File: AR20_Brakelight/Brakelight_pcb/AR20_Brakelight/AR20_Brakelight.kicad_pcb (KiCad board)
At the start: 2 copper layers, 58 parts, among them IC1 PAM2863ECR

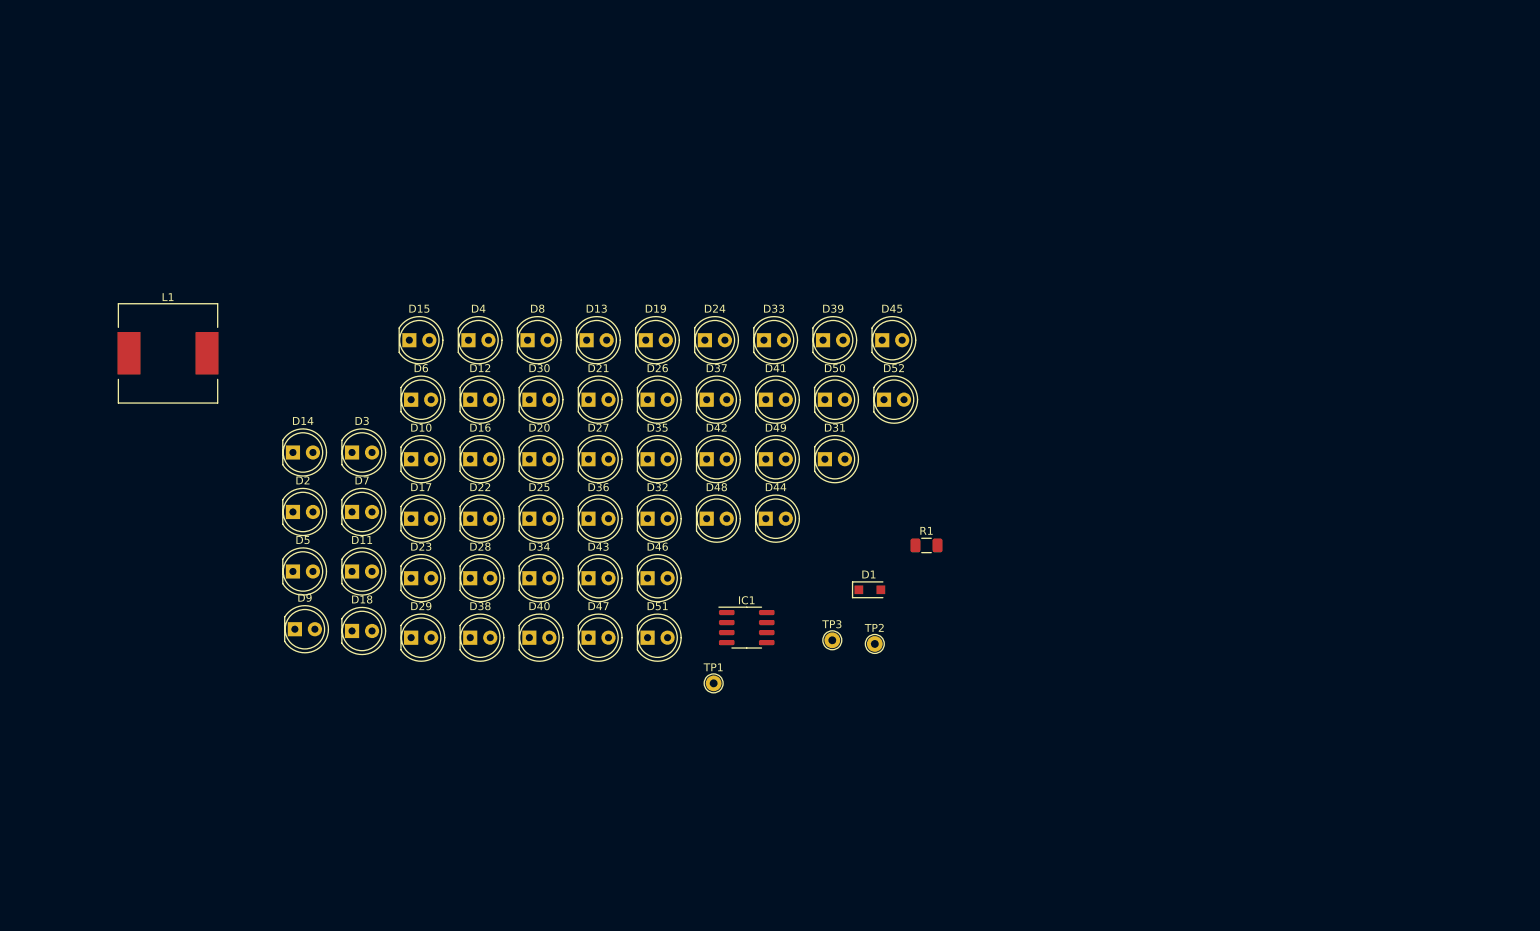
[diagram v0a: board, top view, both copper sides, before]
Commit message: Brakelight PCB 50% ready
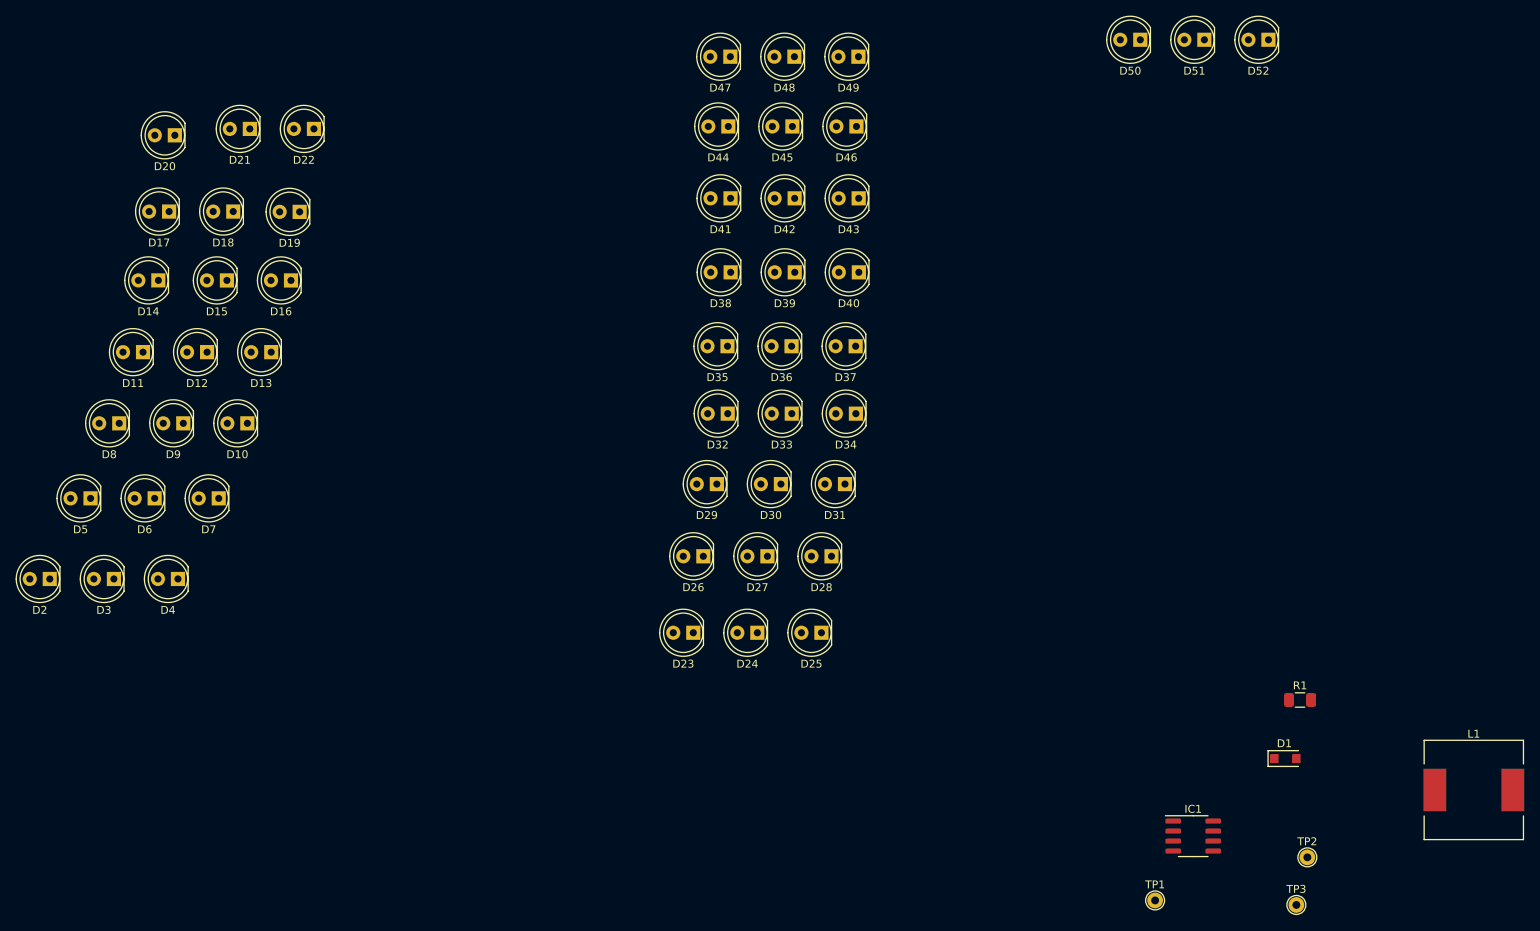
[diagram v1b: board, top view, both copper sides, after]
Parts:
- moved L1 174.7 mm to (257.2, 148.1)
- moved D51 103.7 mm to (223.0, 52.9), turned to 180 degrees
- moved D47 75.9 mm to (162.9, 55.0), turned to 180 degrees
- moved TP3 67.8 mm to (234.7, 162.7)
- moved D52 66.8 mm to (231.2, 52.9), turned to 180 degrees
- moved D46 63.2 mm to (178.9, 63.9), turned to 180 degrees
- moved IC1 62.5 mm to (221.6, 154.0)
- moved D40 62.4 mm to (179.2, 82.4), turned to 180 degrees
- moved TP1 62.4 mm to (216.8, 162.1)
- moved TP2 61.2 mm to (236.1, 156.6)
- moved D20 60.9 mm to (92.4, 65.0), turned to 180 degrees
- moved D50 60.7 mm to (214.9, 52.9), turned to 180 degrees
- moved D48 59.7 mm to (171.0, 55.0), turned to 180 degrees
- moved D43 59.2 mm to (179.2, 73.0), turned to 180 degrees
- moved D38 56.9 mm to (162.9, 82.4), turned to 180 degrees
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
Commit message: Brakelight 80% Ready
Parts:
- moved D49 95.9 mm to (124.0, 133.5), turned to 0 degrees
- moved D52 92.1 mm to (147.3, 91.1), turned to 0 degrees
- moved D48 88.1 mm to (130.7, 133.5), turned to 0 degrees
- moved D46 85.2 mm to (122.3, 127.6), turned to 0 degrees
- moved D47 82.4 mm to (137.5, 133.5), turned to 0 degrees
- moved D25 76.3 mm to (110.2, 86.9), turned to 0 degrees
- moved D43 76.3 mm to (120.6, 121.8), turned to 0 degrees
- moved D51 76.3 mm to (153.2, 83.7)
- moved D45 76.2 mm to (129.0, 127.6), turned to 0 degrees
- moved D50 75.1 mm to (146.3, 83.7)
- moved D44 69.2 mm to (135.8, 127.6), turned to 0 degrees
- moved D40 69.1 mm to (118.8, 116.0), turned to 0 degrees
- moved D28 68.8 mm to (111.9, 92.7), turned to 0 degrees
- moved D42 65.5 mm to (127.3, 121.8), turned to 0 degrees
- moved D31 64.7 mm to (113.7, 98.5), turned to 0 degrees
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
